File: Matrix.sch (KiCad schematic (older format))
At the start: 171 parts

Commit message: Add ISO/Small Enter, Update netlist
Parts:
- added K_ISOENTER1: MX-ISO, MX_Alps_Hybrid:MX-1U, symbol MX-ISO
- added K_SENTER1: MX-1.25U, MX_Alps_Hybrid:MX-1U, symbol MX-1.25U
- K_BACK1: value MX-1U -> MX-2U; symbol MX-1U -> MX-2U
- K_ENTER1: value MX-1U -> MX-2.25U; symbol MX-1U -> MX-2.25U
- K_\1: value MX-1U -> MX-1.5U; symbol MX-1U -> MX-1.5U
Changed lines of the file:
@@
 $EndComp
 $Comp
-L MX-1U K_\1
+L MX-1.5U K_\1
 U 1 1 597E3C69
 P 13100 3125
 F 0 "K_\\1" H 13100 3250 60  0000 C CNN
-F 1 "MX-1U" H 13100 3175 20  0000 C CNN
+F 1 "MX-1.5U" H 13100 3175 20  0000 C CNN
 F 2 "MX_Alps_Hybrid:MX-1U" H 13075 3100 60  0001 C CNN
 F 3 "" H 13075 3100 60  0001 C CNN
@@
 $EndComp
 $Comp
-L MX-1U K_ENTER1
+L MX-2.25U K_ENTER1
 U 1 1 597E5DA9
 P 13100 3675
 F 0 "K_ENTER1" H 13100 3800 60  0000 C CNN
-F 1 "MX-1U" H 13100 3725 20  0000 C CNN
+F 1 "MX-2.25U" H 13100 3725 20  0000 C CNN
 F 2 "MX_Alps_Hybrid:MX-1U" H 13075 3650 60  0001 C CNN
 F 3 "" H 13075 3650 60  0001 C CNN
@@
 $EndComp
 $Comp
-L MX-1U K_BACK1
+L MX-2U K_BACK1
 U 1 1 59800CF4
 P 12400 2025
 F 0 "K_BACK1" H 12400 2150 60  0000 C CNN
-F 1 "MX-1U" H 12400 2075 20  0000 C CNN
+F 1 "MX-2U" H 12400 2075 20  0000 C CNN
 F 2 "MX_Alps_Hybrid:MX-1U" H 12375 2000 60  0001 C CNN
 F 3 "" H 12375 2000 60  0001 C CNN
@@
 	3850 2600 3850 1300
 Connection ~ 4550 1300
+$Comp
+L MX-ISO K_ISOENTER1
+U 1 1 597E38AB
+P 13100 4225
+F 0 "K_ISOENTER1" H 13100 4350 60  0000 C CNN
+F 1 "MX-ISO" H 13100 4275 20  0000 C CNN
+F 2 "MX_Alps_Hybrid:MX-1U" H 13075 4200 60  0001 C CNN
+F 3 "" H 13075 4200 60  0001 C CNN
+	1    13100 4225
+	1    0    0    -1
+$EndComp
+$Comp
+L MX-1.25U K_SENTER1
+U 1 1 597EB602
+P 13100 4775
+F 0 "K_SENTER1" H 13100 4900 60  0000 C CNN
+F 1 "MX-1.25U" H 13100 4825 20  0000 C CNN
+F 2 "MX_Alps_Hybrid:MX-1U" H 13075 4750 60  0001 C CNN
+F 3 "" H 13075 4750 60  0001 C CNN
+	1    13100 4775
+	1    0    0    -1
+$EndComp
 $EndSCHEMATC

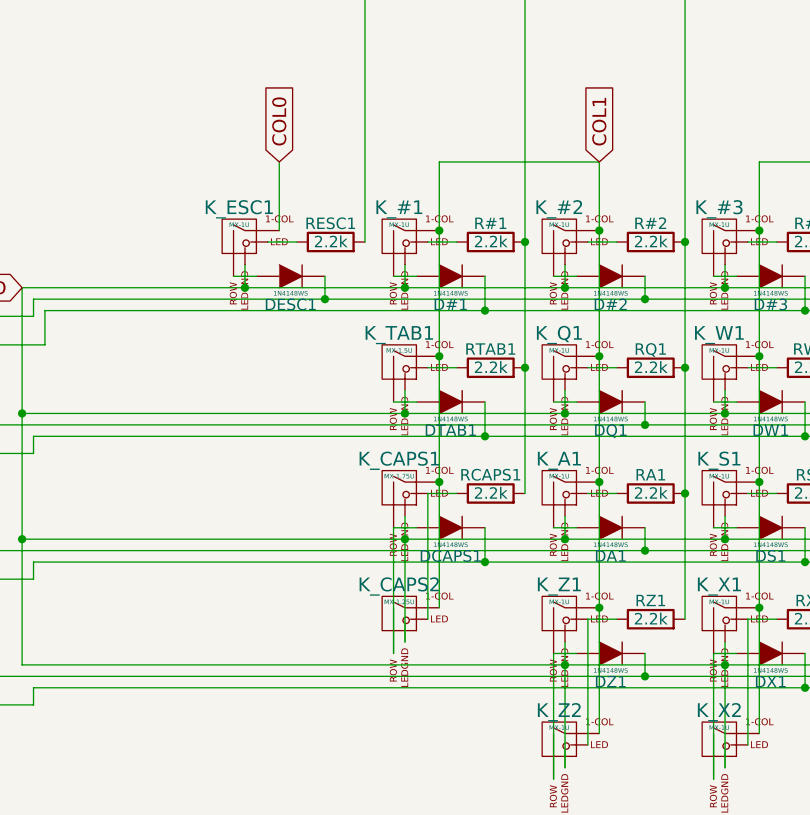
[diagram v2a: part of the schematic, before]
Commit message: Fix caps wiring and update netlist
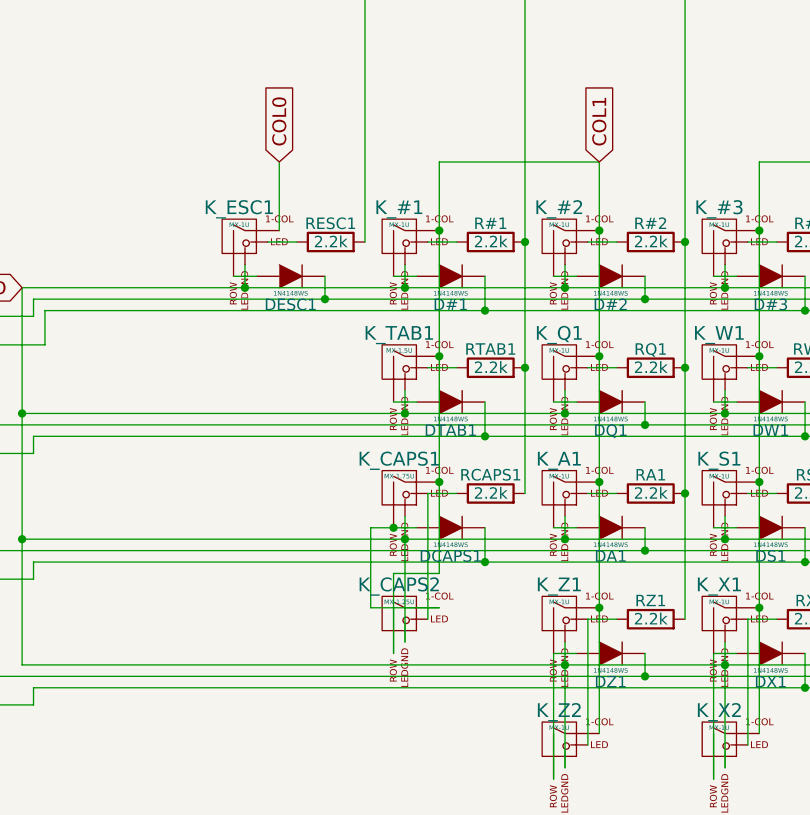
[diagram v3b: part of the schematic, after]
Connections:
- net COL1: now also K_CAPS2.2 (ROW); no longer K_CAPS2.1 (COL)
- net at DCAPS1.2 (A), K_CAPS1.2 (ROW): now also K_CAPS2.1 (COL); no longer K_CAPS2.2 (ROW)
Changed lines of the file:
@@
 	4250 3700 4125 3700
 Wire Wire Line
-	3975 3850 4075 3850
+	3875 3850 4075 3850
 Wire Wire Line
 	4950 3700 4825 3700
@@
 	4875 2250 4175 2250
 Wire Wire Line
-	4175 2250 4175 4200
+	4175 2250 4175 4050
 Connection ~ 4875 2550
 Connection ~ 4175 2550
@@
 	4725 4350 4725 4900
 Connection ~ 5425 4450
-Wire Wire Line
-	3975 4400 3975 3850
 Connection ~ 4025 3900
 Wire Wire Line
@@
 	1    0    0    -1
 $EndComp
+Wire Wire Line
+	4175 4050 3975 4050
+Wire Wire Line
+	3975 4050 3975 4400
+Wire Wire Line
+	4175 4200 3875 4200
+Wire Wire Line
+	3875 4200 3875 3850
+Connection ~ 3975 3850
 $EndSCHEMATC

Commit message: Fix first batch of wrong size footprints
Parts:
- K_BACK1: footprint MX_Alps_Hybrid:MX-1U -> MX_Alps_Hybrid:MX-2U
- K_CAPS1: footprint MX_Alps_Hybrid:MX-1U -> MX_Alps_Hybrid:MX-1.75U
- K_CAPS2: footprint MX_Alps_Hybrid:MX-1U -> MX_Alps_Hybrid:MX-1.25U
- K_ENTER1: footprint MX_Alps_Hybrid:MX-1U -> MX_Alps_Hybrid:MX-2.25U
- K_ISOENTER1: footprint MX_Alps_Hybrid:MX-1U -> MX_Alps_Hybrid:MX-ISO-Combined
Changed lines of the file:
@@
 F 0 "K_CAPS1" H 4000 3800 60  0000 C CNN
 F 1 "MX-1.75U" H 4000 3725 20  0000 C CNN
-F 2 "MX_Alps_Hybrid:MX-1U" H 3975 3650 60  0001 C CNN
+F 2 "MX_Alps_Hybrid:MX-1.75U" H 3975 3650 60  0001 C CNN
 F 3 "" H 3975 3650 60  0001 C CNN
 	1    4000 3675
@@
 F 0 "K_ENTER1" H 13100 3800 60  0000 C CNN
 F 1 "MX-2.25U" H 13100 3725 20  0000 C CNN
-F 2 "MX_Alps_Hybrid:MX-1U" H 13075 3650 60  0001 C CNN
+F 2 "MX_Alps_Hybrid:MX-2.25U" H 13075 3650 60  0001 C CNN
 F 3 "" H 13075 3650 60  0001 C CNN
 	1    13100 3675
@@
 F 0 "K_CAPS2" H 4000 4350 60  0000 C CNN
 F 1 "MX-1.25U" H 4000 4275 20  0000 C CNN
-F 2 "MX_Alps_Hybrid:MX-1U" H 3975 4200 60  0001 C CNN
+F 2 "MX_Alps_Hybrid:MX-1.25U" H 3975 4200 60  0001 C CNN
 F 3 "" H 3975 4200 60  0001 C CNN
 	1    4000 4225
@@
 F 0 "K_BACK1" H 12400 2150 60  0000 C CNN
 F 1 "MX-2U" H 12400 2075 20  0000 C CNN
-F 2 "MX_Alps_Hybrid:MX-1U" H 12375 2000 60  0001 C CNN
+F 2 "MX_Alps_Hybrid:MX-2U" H 12375 2000 60  0001 C CNN
 F 3 "" H 12375 2000 60  0001 C CNN
 	1    12400 2025
@@
 F 0 "K_ISOENTER1" H 13100 4350 60  0000 C CNN
 F 1 "MX-ISO" H 13100 4275 20  0000 C CNN
-F 2 "MX_Alps_Hybrid:MX-1U" H 13075 4200 60  0001 C CNN
+F 2 "MX_Alps_Hybrid:MX-ISO-Combined" H 13075 4200 60  0001 C CNN
 F 3 "" H 13075 4200 60  0001 C CNN
 	1    13100 4225

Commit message: Fix wrong size footprints (Hopefully all of them)
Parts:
- K_TAB1, K_\1: footprint MX_Alps_Hybrid:MX-1U -> MX_Alps_Hybrid:MX-1.5U
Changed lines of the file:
@@
 F 0 "K_TAB1" H 4000 3250 60  0000 C CNN
 F 1 "MX-1.5U" H 4000 3175 20  0000 C CNN
-F 2 "MX_Alps_Hybrid:MX-1U" H 3975 3100 60  0001 C CNN
+F 2 "MX_Alps_Hybrid:MX-1.5U" H 3975 3100 60  0001 C CNN
 F 3 "" H 3975 3100 60  0001 C CNN
 	1    4000 3125
@@
 F 0 "K_\\1" H 13100 3250 60  0000 C CNN
 F 1 "MX-1.5U" H 13100 3175 20  0000 C CNN
-F 2 "MX_Alps_Hybrid:MX-1U" H 13075 3100 60  0001 C CNN
+F 2 "MX_Alps_Hybrid:MX-1.5U" H 13075 3100 60  0001 C CNN
 F 3 "" H 13075 3100 60  0001 C CNN
 	1    13100 3125

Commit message: Assign the footprints for every resistor and diode
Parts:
- D#0_1, D#1, D#2, D#3, D#4, D#5, D#6, D#7, D#8, D#9, D'1, D,1, D-1, D.1, D;1, D=1, D?1, DA1, DB1, DC1, DCAPS1, DD1, DDEL1, DE1, DENTER1, DESC1, DF1, DG1, DH1, DI1, DISO`1, DJ1, DK1, DL1, DM1, DN1, DO1, DP1, DQ1, DR1, DS1, DSBACK1, DT1, DTAB1, DU1, DV1, DW1, DX1, DY1, DZ1, D[1, D\1, D]1: footprint (none) -> Diodes_SMD:D_SOD-323
- R#0_1, R#1, R#2, R#3, R#4, R#5, R#6, R#7, R#8, R#9, R'1, R,1, R-1, R.1, R;1, R=1, R?1, RA1, RB1, RC1, RCAPS1, RD1, RDEL1, RE1, RENTER1, RESC1, RF1, RG1, RH1, RI1, RISO`1, RJ1, RK1, RL1, RM1, RN1, RO1, RP1, RQ1, RR1, RS1, RSBACK1, RT1, RTAB1, RU1, RV1, RW1, RX1, RY1, RZ1, R[1, R\1, R]1: footprint (none) -> Resistors_SMD:R_0603

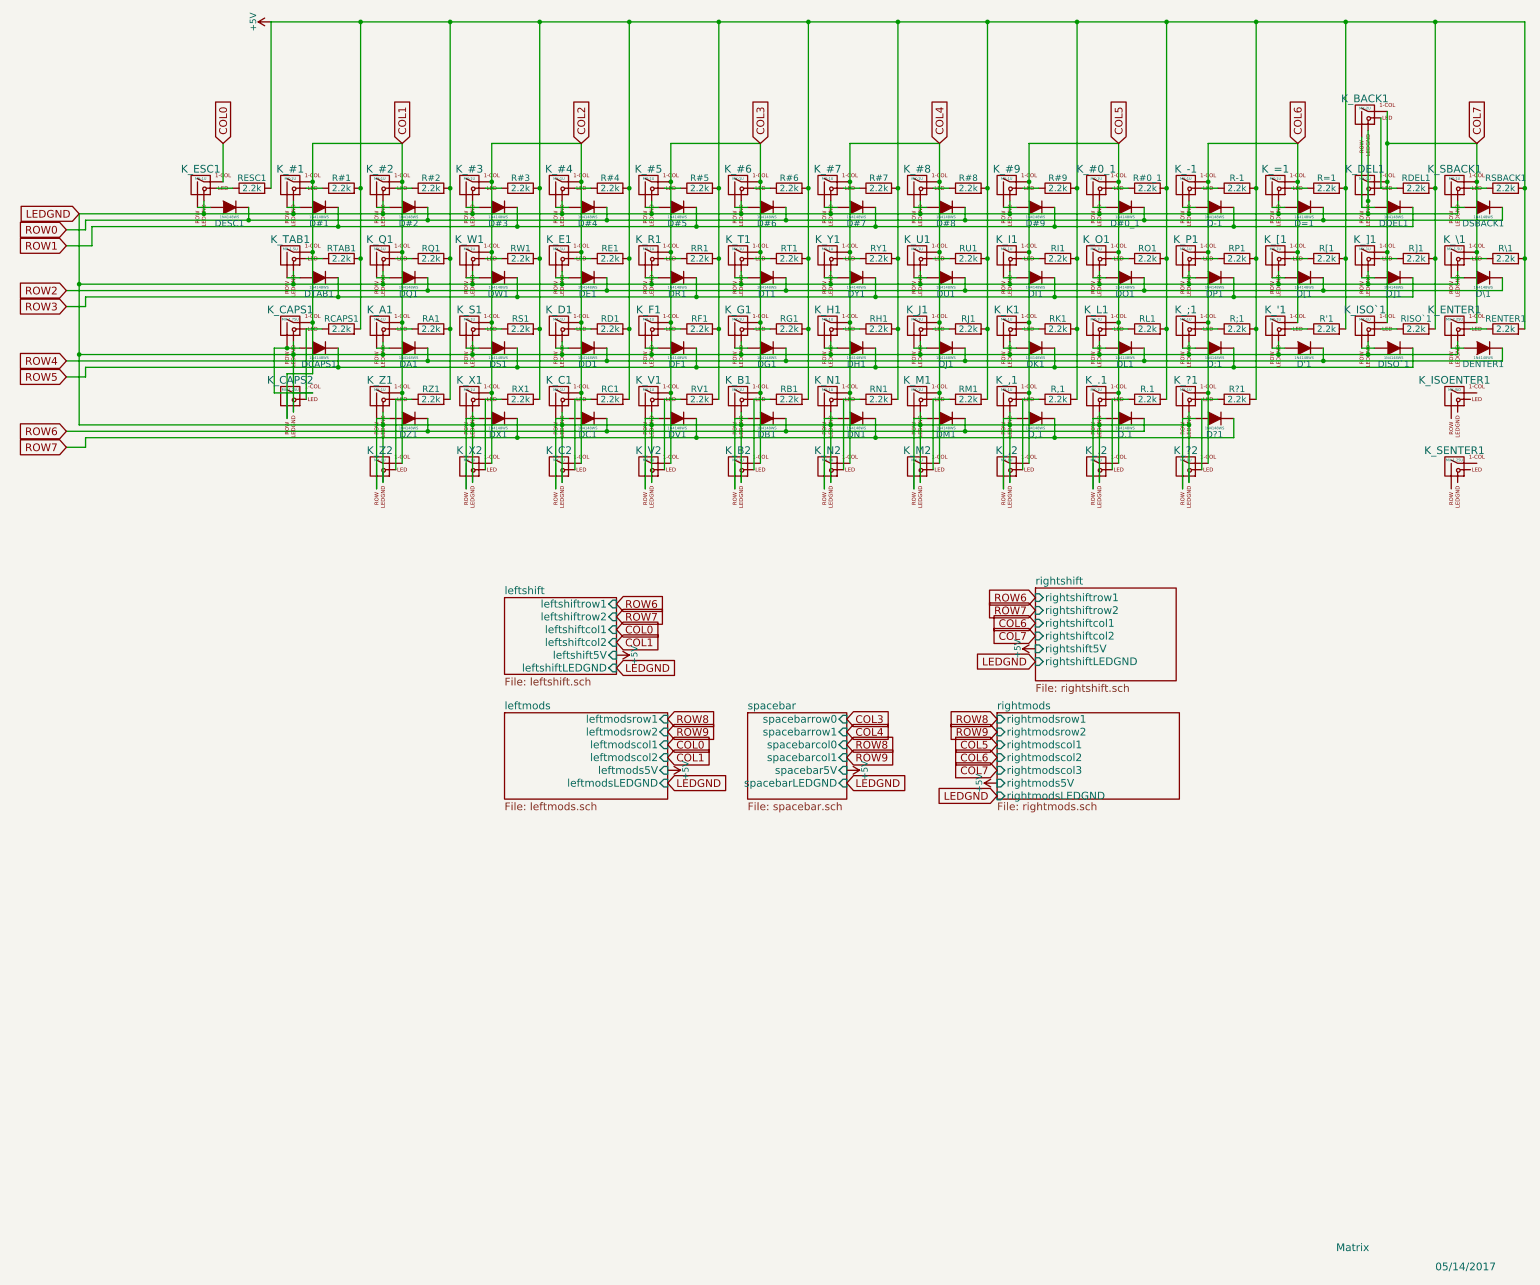
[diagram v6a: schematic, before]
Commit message: Flipped schematic symbols for keys (except LS and bottom right mods)
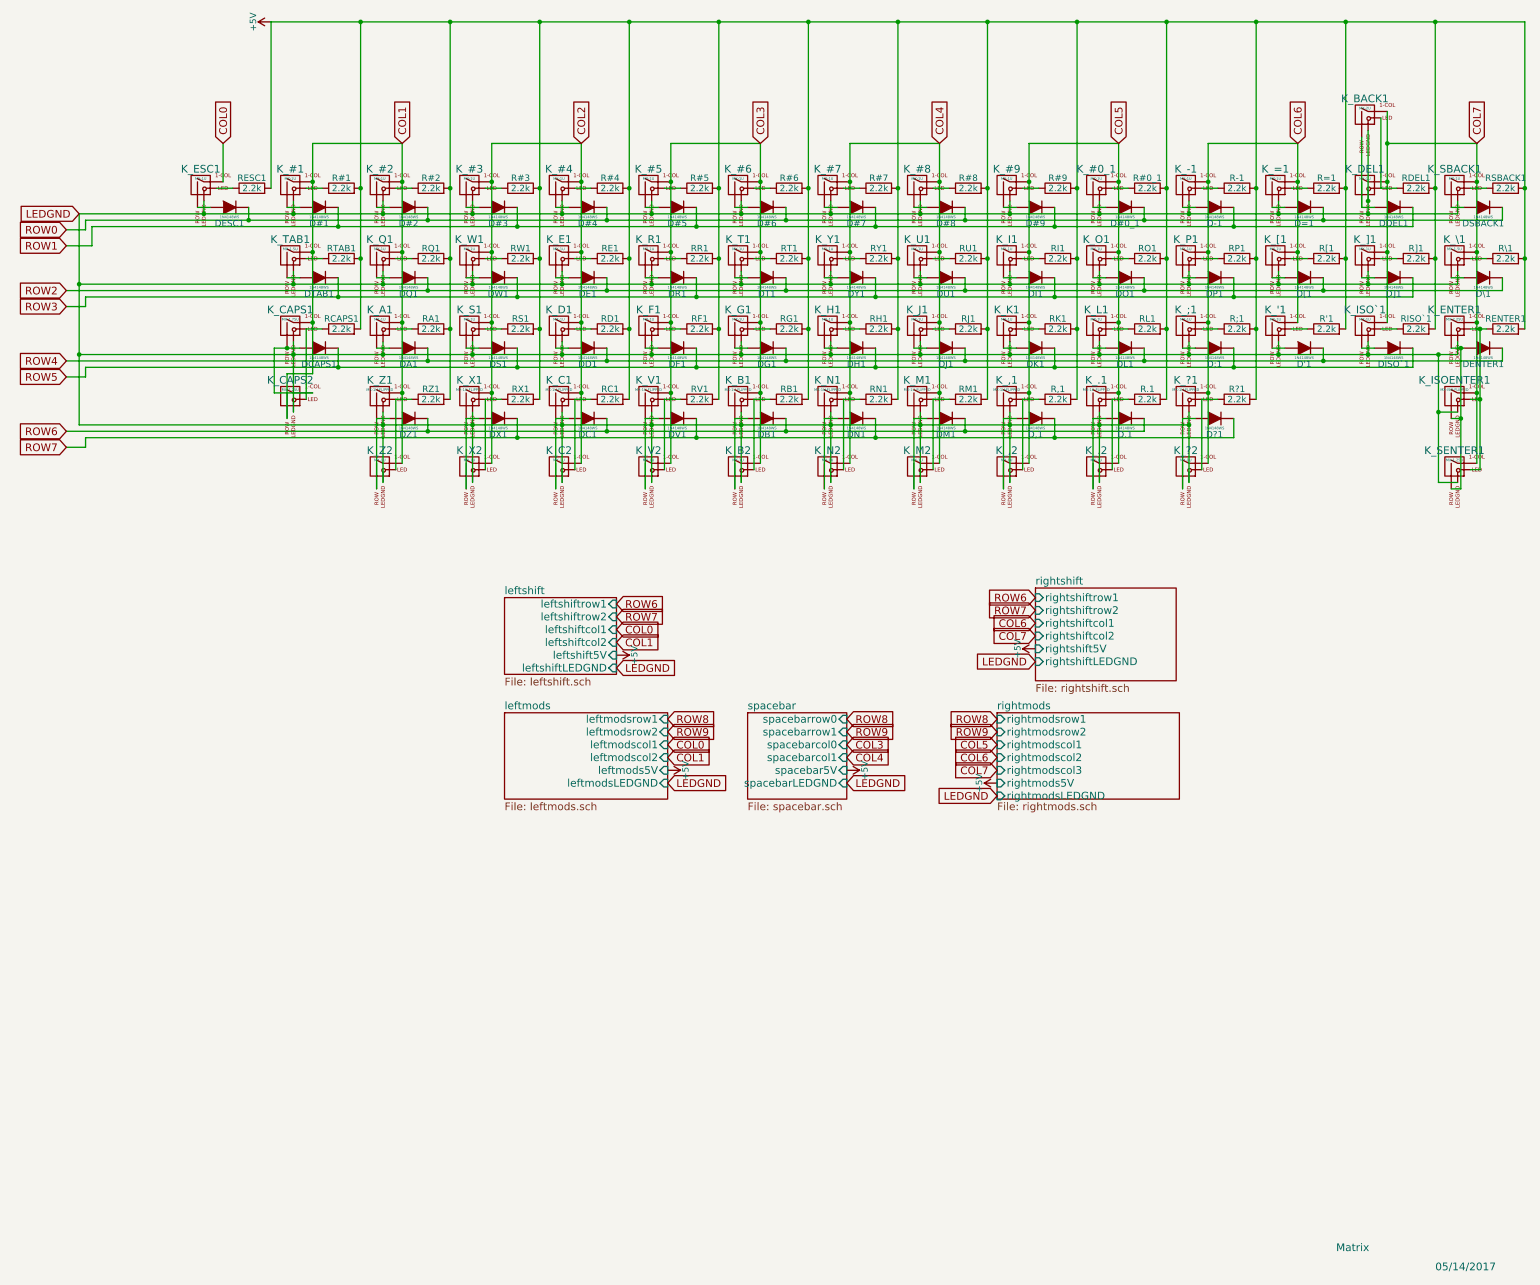
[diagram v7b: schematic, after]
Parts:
- removed K_,1, K_.1, K_?1, K_B1, K_C1, K_M1, K_N1, K_V1, K_X1, K_Z1: MX-1U, MX_Alps_Hybrid:MX-1U, symbol MX-1U
- removed K_ISOENTER1: MX-ISO, MX_Alps_Hybrid:MX-ISO-Combined, symbol MX-ISO
- added K_,1, K_.1, K_?1, K_B1, K_C1, K_M1, K_N1, K_V1, K_X1, K_Z1: MX-1U-FLIPPED, symbol MX-1U-FLIPPED
- added K_ISOENTER1: MX-ISO-FLIPPED, symbol MX-ISO-FLIPPED
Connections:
- net COL1: now also K_Z1.2 (COL)
- net COL2: now also K_C1.2 (COL), K_X1.2 (COL)
- net COL3: now also K_B1.2 (COL), K_V1.2 (COL)
- net COL4: now also K_M1.2 (COL), K_N1.2 (COL)
- net COL5: now also K_,1.2 (COL), K_.1.2 (COL)
- net COL6: now also K_?1.2 (COL)
- net COL7: now also K_SENTER1.1 (COL), K_ISOENTER1.2 (COL)
- net LEDGND: now also K_SENTER1.4 (LEDGND), K_,1.4 (LEDGND), K_.1.4 (LEDGND), K_?1.4 (LEDGND), K_B1.4 (LEDGND), K_C1.4 (LEDGND), K_ISOENTER1.4 (LEDGND), K_M1.4 (LEDGND), K_N1.4 (LEDGND), K_V1.4 (LEDGND), K_X1.4 (LEDGND), K_Z1.4 (LEDGND)
- net at DENTER1.2 (A), K_ENTER1.2 (ROW): now also K_SENTER1.2 (ROW), K_ISOENTER1.1 (ROW)
- net at K_ENTER1.3 (LED), RENTER1.1: now also K_SENTER1.3 (LED), K_ISOENTER1.3 (LED)
- net at DZ1.2 (A), K_Z2.2 (ROW): now also K_Z1.1 (ROW)
- net at K_Z2.3 (LED), RZ1.1: now also K_Z1.3 (LED)
- net at DX1.2 (A), K_X2.2 (ROW): now also K_X1.1 (ROW)
- net at K_X2.3 (LED), RX1.1: now also K_X1.3 (LED)
- net at DC1.2 (A), K_C2.2 (ROW): now also K_C1.1 (ROW)
- net at K_C2.3 (LED), RC1.1: now also K_C1.3 (LED)
- net at DV1.2 (A), K_V2.2 (ROW): now also K_V1.1 (ROW)
- net at K_V2.3 (LED), RV1.1: now also K_V1.3 (LED)
- net at DB1.2 (A), K_B2.2 (ROW): now also K_B1.1 (ROW)
- net at K_B2.3 (LED), RB1.1: now also K_B1.3 (LED)
- net at DN1.2 (A), K_N2.2 (ROW): now also K_N1.1 (ROW)
- net at K_N2.3 (LED), RN1.1: now also K_N1.3 (LED)
- net at DM1.2 (A), K_M2.2 (ROW): now also K_M1.1 (ROW)
- net at K_M2.3 (LED), RM1.1: now also K_M1.3 (LED)
- net at D,1.2 (A), K_,2.2 (ROW): now also K_,1.1 (ROW)
- net at K_,2.3 (LED), R,1.1: now also K_,1.3 (LED)
- net at D.1.2 (A), K_.2.2 (ROW): now also K_.1.1 (ROW)
- net at K_.2.3 (LED), R.1.1: now also K_.1.3 (LED)
- net at D?1.2 (A), K_?2.2 (ROW): now also K_?1.1 (ROW)
- net at K_?2.3 (LED), R?1.2: now also K_?1.3 (LED)

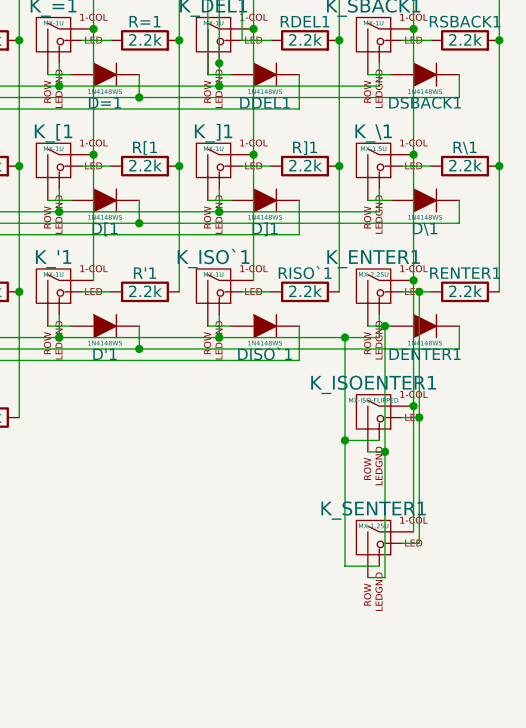
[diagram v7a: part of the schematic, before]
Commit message: Wired some leds
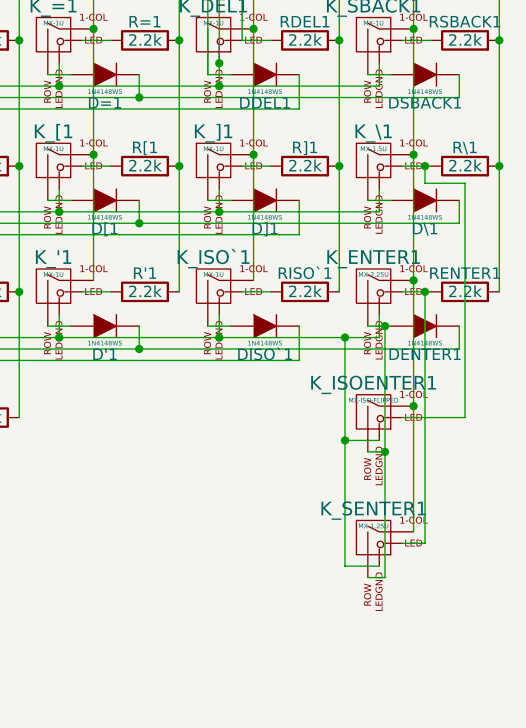
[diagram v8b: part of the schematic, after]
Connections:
- net at K_\1.3 (LED), R\1.1: now also K_ISOENTER1.3 (LED)
- net at K_ENTER1.3 (LED), K_SENTER1.3 (LED), RENTER1.1: no longer K_ISOENTER1.3 (LED)
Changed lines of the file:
@@
 	12375 3850 12475 3850
 Wire Wire Line
-	13350 3700 13225 3700
+	13225 3700 13350 3700
 Wire Wire Line
 	13075 3850 13175 3850
@@
 Connection ~ 13275 4200
 Wire Wire Line
-	13225 4800 13300 4800
-Wire Wire Line
-	13300 4800 13300 3700
-Connection ~ 13300 3700
-Wire Wire Line
-	13225 4250 13300 4250
-Connection ~ 13300 4250
-Wire Wire Line
-	13125 4900 12975 4900
-Wire Wire Line
-	12975 4900 12975 3900
+	13225 4800 13325 4800
+Wire Wire Line
+	12975 4900 13125 4900
+Wire Wire Line
+	12975 3900 12975 4900
 Connection ~ 12975 3900
 Wire Wire Line
@@
 	1    0    0    -1
 $EndComp
+Wire Wire Line
+	13325 4800 13325 3700
+Connection ~ 13325 3700
+Wire Wire Line
+	13225 4250 13500 4250
+Wire Wire Line
+	13500 4250 13500 3225
+Wire Wire Line
+	13500 3225 13325 3225
+Wire Wire Line
+	13325 3225 13325 3150
+Connection ~ 13325 3150
 $EndSCHEMATC
